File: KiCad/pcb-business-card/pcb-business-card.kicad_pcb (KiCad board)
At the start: 2 copper layers, 0 parts

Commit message: Add board outline
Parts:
- added G***: LOGO, LOGO, F.Cu at (149.6, 99.5)
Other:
- board outline added: 85.5 x 53.9 mm
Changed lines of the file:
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@@
   )
   (net 0 "")
+  (footprint "LOGO" (layer "F.Cu")
+    (at 149.64 99.5)
+    (attr through_hole)
+    (fp_text reference "G***" (at 0 0) (layer "F.SilkS") hide
+      (effects (font (size 1.524 1.524) (thickness 0.3)))
+    )
+    (fp_text value "LOGO" (at 0.75 0) (layer "F.SilkS") hide
+      (effects (font (size 1.524 1.524) (thickness 0.3)))
+    )
+  )
+  (gr_arc (start 190.54 75.6) (mid 192.307767 76.332233) (end 193.04 78.1) (layer "Edge.Cuts") (width 0.15))
+  (gr_arc (start 110.04 129.5) (mid 108.272233 128.767767) (end 107.54 127) (layer "Edge.Cuts") (width 0.15))
+  (gr_arc (start 193.04 127) (mid 192.307767 128.767767) (end 190.54 129.5) (layer "Edge.Cuts") (width 0.15))
+  (gr_line (start 110.04 129.5) (end 190.54 129.5) (layer "Edge.Cuts") (width 0.15))
+  (gr_line (start 107.54 78.1) (end 107.54 127) (layer "Edge.Cuts") (width 0.15))
+  (gr_line (start 190.54 75.6) (end 110.04 75.6) (layer "Edge.Cuts") (width 0.15))
+  (gr_arc (start 107.54 78.1) (mid 108.272233 76.332233) (end 110.04 75.6) (layer "Edge.Cuts") (width 0.15))
+  (gr_line (start 193.04 127) (end 193.04 78.1) (layer "Edge.Cuts") (width 0.15))
 )

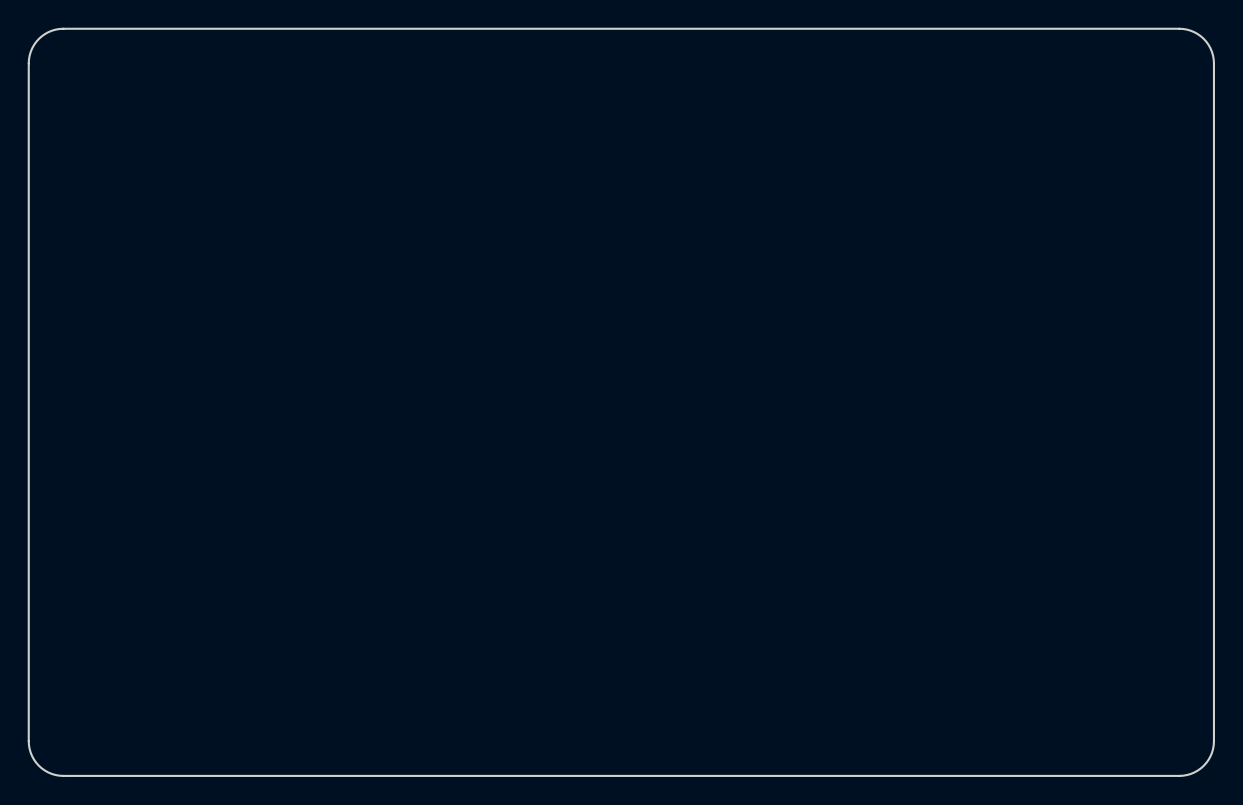
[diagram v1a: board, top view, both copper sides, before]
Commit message: Finish PCB layout
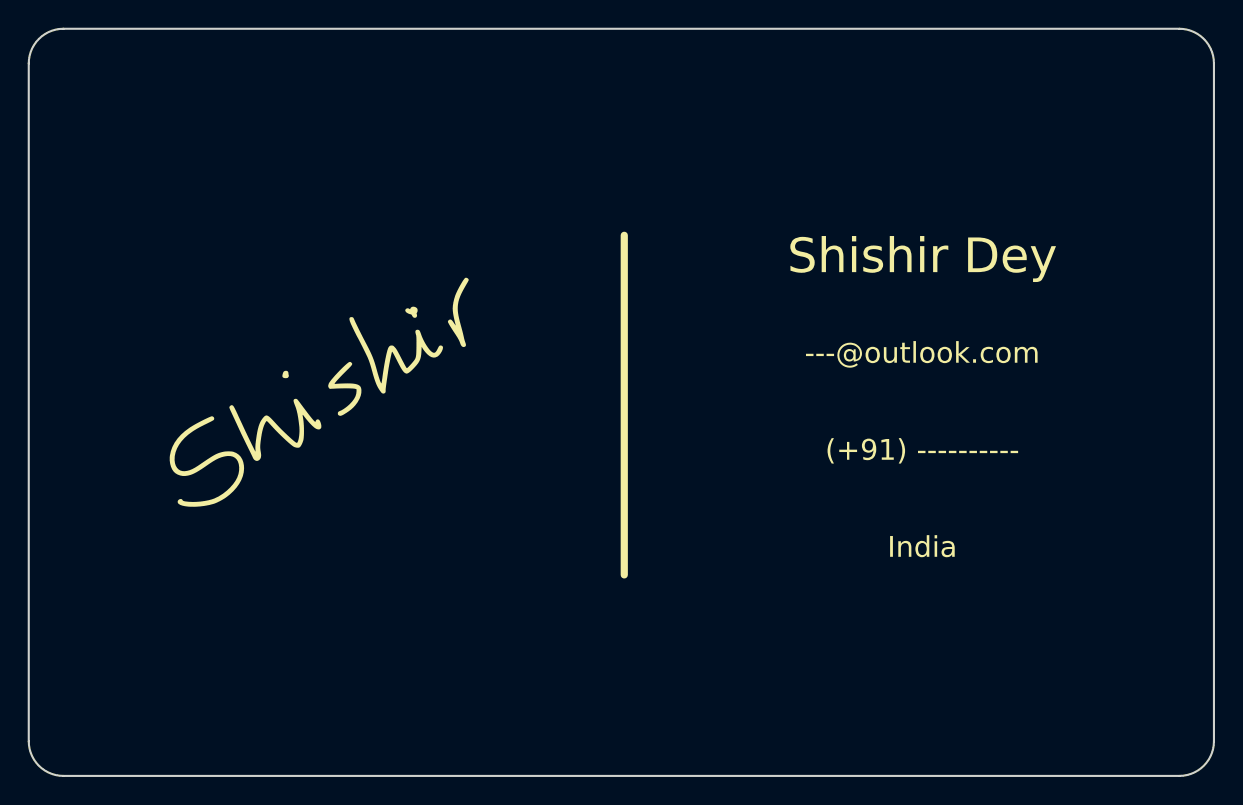
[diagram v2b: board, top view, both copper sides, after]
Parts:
- added G***: LOGO, Custom:shishir-sign, F.Cu at (129.0, 102.5)
- added G***: LOGO, Custom:shishir-portfolio-qr-code, B.Cu at (171.5, 103.0)
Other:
- board text added: "(+91) ----------"
- board text added: "---@outlook.com"
- board text added: "India"
- board text added: "Portfolio"
- board text added: "Shishir Dey"
- board text added: "Works with"
- board text added: "• Firmware Development"
- board text added: "• PCB Designing"
- board text added: "• PLC and HMI programming"
- board text added: "• Power Electronics"
- board text added: "• Web Development"
